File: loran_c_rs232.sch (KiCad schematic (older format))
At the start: 30 parts, among them P301 UART1 3V3, P302 DB9 Ribbon 1, P303 DB9 Ribbon 2, U301 ST3232, U302 ST3232, U303 ST3232

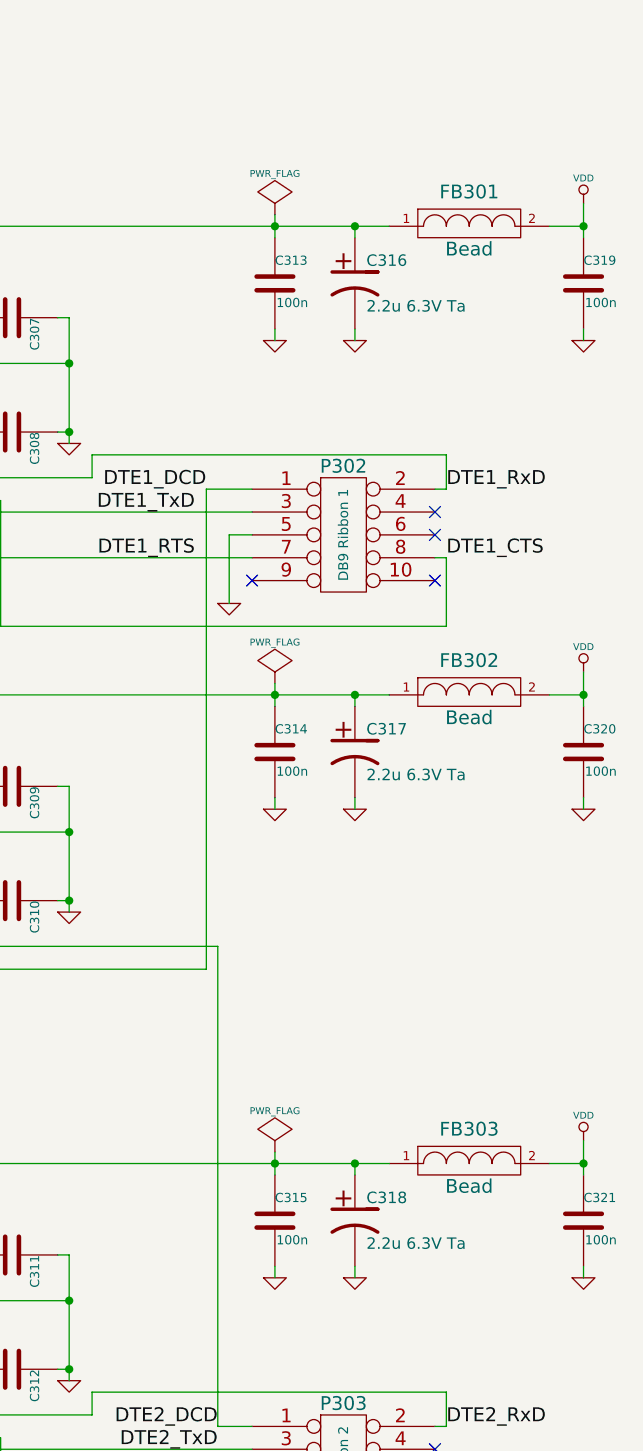
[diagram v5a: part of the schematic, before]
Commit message: Intermediate update: PCB routing/schematic tweaking in process..
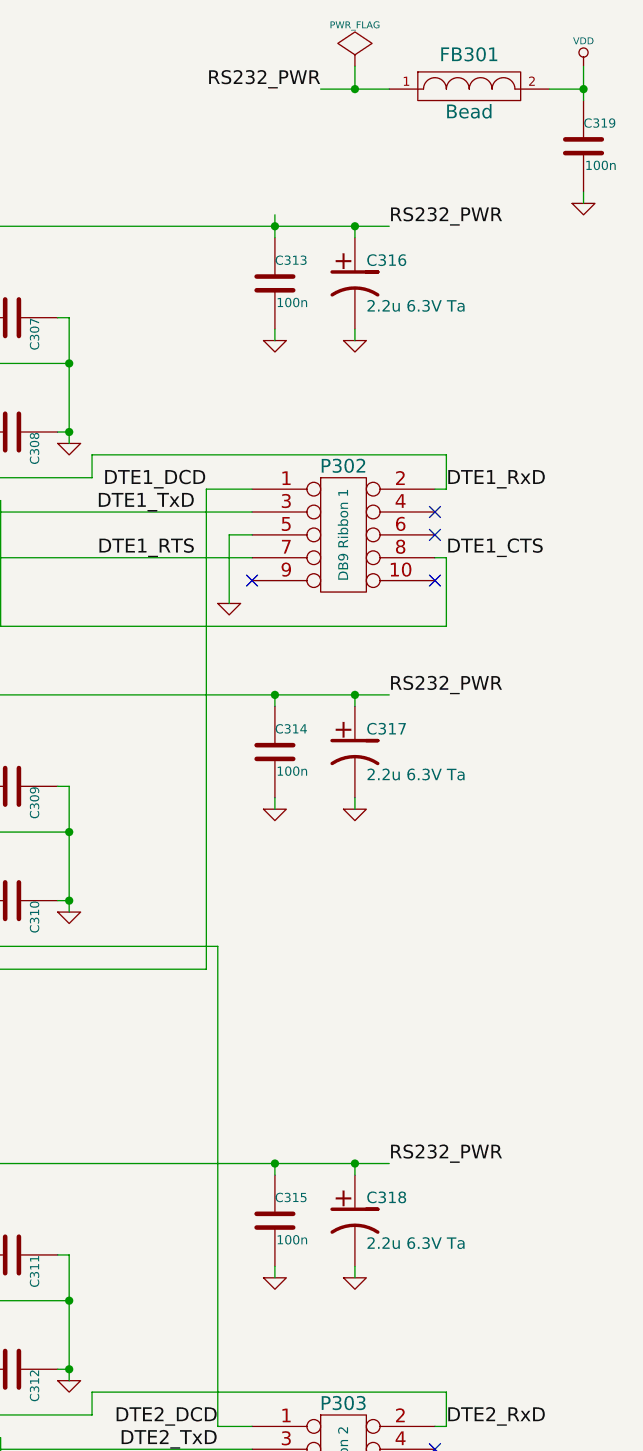
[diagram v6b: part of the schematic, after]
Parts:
- removed C320, C321: 100n, w_smd_capacitors:c_1206, symbol C
- removed FB302, FB303: Bead, w_pth_resistors:RC07, symbol FILTER
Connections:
- net RS232_PWR: now reaches C313.1, C316.1, FB301.1, U301.16 (VCC)
- net RS232_PWR: now also C314.1, C315.1, C317.1, C318.1, U302.16 (VCC), U303.16 (VCC)
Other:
- moved on the sheet: C319, FB301
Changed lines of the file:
@@
 DTE2_CTS
 $Comp
-L GND #PWR057
+L GND #PWR061
 U 1 1 52DBAE37
 P 5600 7750
-F 0 "#PWR057" H 5600 7750 30  0001 C CNN
+F 0 "#PWR061" H 5600 7750 30  0001 C CNN
 F 1 "GND" H 5600 7680 30  0001 C CNN
 F 2 "" H 5600 7750 60  0000 C CNN
@@
 DTE1_CTS
 $Comp
-L GND #PWR058
+L GND #PWR062
 U 1 1 52DBB093
 P 5600 3650
-F 0 "#PWR058" H 5600 3650 30  0001 C CNN
+F 0 "#PWR062" H 5600 3650 30  0001 C CNN
 F 1 "GND" H 5600 3580 30  0001 C CNN
 F 2 "" H 5600 3650 60  0000 C CNN
@@
 $EndComp
 $Comp
-L GND #PWR059
+L GND #PWR063
 U 1 1 52DBC5A6
 P 4900 2950
-F 0 "#PWR059" H 4900 2950 30  0001 C CNN
+F 0 "#PWR063" H 4900 2950 30  0001 C CNN
 F 1 "GND" H 4900 2880 30  0001 C CNN
 F 2 "" H 4900 2950 60  0000 C CNN
@@
 $EndComp
 $Comp
-L GND #PWR060
+L GND #PWR064
 U 1 1 52DBD4A5
 P 4900 7050
-F 0 "#PWR060" H 4900 7050 30  0001 C CNN
+F 0 "#PWR064" H 4900 7050 30  0001 C CNN
 F 1 "GND" H 4900 6980 30  0001 C CNN
 F 2 "" H 4900 7050 60  0000 C CNN
@@
 $EndComp
 $Comp
-L GND #PWR061
+L GND #PWR065
 U 1 1 52DBD9EF
 P 4900 5000
-F 0 "#PWR061" H 4900 5000 30  0001 C CNN
+F 0 "#PWR065" H 4900 5000 30  0001 C CNN
 F 1 "GND" H 4900 4930 30  0001 C CNN
 F 2 "" H 4900 5000 60  0000 C CNN
@@
 $EndComp
 $Comp
-L GND #PWR062
+L GND #PWR066
 U 1 1 52DC08D0
 P 5800 2500
-F 0 "#PWR062" H 5800 2500 30  0001 C CNN
+F 0 "#PWR066" H 5800 2500 30  0001 C CNN
 F 1 "GND" H 5800 2430 30  0001 C CNN
 F 2 "" H 5800 2500 60  0000 C CNN
@@
 $EndComp
 $Comp
-L GND #PWR063
+L GND #PWR067
 U 1 1 52DC08DB
 P 6150 2500
-F 0 "#PWR063" H 6150 2500 30  0001 C CNN
+F 0 "#PWR067" H 6150 2500 30  0001 C CNN
 F 1 "GND" H 6150 2430 30  0001 C CNN
 F 2 "" H 6150 2500 60  0000 C CNN
@@
 L FILTER FB301
 U 1 1 52DC0EC1
-P 6650 2000
-F 0 "FB301" H 6650 2150 60  0000 C CNN
-F 1 "Bead" H 6650 1900 60  0000 C CNN
-F 2 "w_pth_resistors:RC07" H 6650 2000 60  0001 C CNN
-F 3 "" H 6650 2000 60  0000 C CNN
-	1    6650 2000
+P 6650 1400
+F 0 "FB301" H 6650 1550 60  0000 C CNN
+F 1 "Bead" H 6650 1300 60  0000 C CNN
+F 2 "w_pth_resistors:RC07" H 6650 1400 60  0001 C CNN
+F 3 "" H 6650 1400 60  0000 C CNN
+	1    6650 1400
 	1    0    0    -1
 $EndComp
@@
 L C C319
 U 1 1 52DC0F4D
-P 7150 2250
-F 0 "C319" H 7150 2350 40  0000 L CNN
-F 1 "100n" H 7156 2165 40  0000 L CNN
-F 2 "w_smd_capacitors:c_1206" H 7188 2100 30  0001 C CNN
-F 3 "" H 7150 2250 60  0000 C CNN
-	1    7150 2250
-	1    0    0    -1
-$EndComp
-$Comp
-L GND #PWR064
+P 7150 1650
+F 0 "C319" H 7150 1750 40  0000 L CNN
+F 1 "100n" H 7156 1565 40  0000 L CNN
+F 2 "w_smd_capacitors:c_1206" H 7188 1500 30  0001 C CNN
+F 3 "" H 7150 1650 60  0000 C CNN
+	1    7150 1650
+	1    0    0    -1
+$EndComp
+$Comp
+L GND #PWR068
 U 1 1 52DC0F53
-P 7150 2500
-F 0 "#PWR064" H 7150 2500 30  0001 C CNN
-F 1 "GND" H 7150 2430 30  0001 C CNN
-F 2 "" H 7150 2500 60  0000 C CNN
-F 3 "" H 7150 2500 60  0000 C CNN
-	1    7150 2500
-	1    0    0    -1
-$EndComp
-Wire Wire Line
-	7150 2450 7150 2500
-Wire Wire Line
-	7000 2000 7150 2000
-Wire Wire Line
-	7150 1900 7150 2050
-Connection ~ 7150 2000
-$Comp
-L VDD #PWR065
-U 1 1 52DC1066
 P 7150 1900
-F 0 "#PWR065" H 7150 2000 30  0001 C CNN
-F 1 "VDD" H 7150 2010 30  0000 C CNN
+F 0 "#PWR068" H 7150 1900 30  0001 C CNN
+F 1 "GND" H 7150 1830 30  0001 C CNN
 F 2 "" H 7150 1900 60  0000 C CNN
 F 3 "" H 7150 1900 60  0000 C CNN
 	1    7150 1900
+	1    0    0    -1
+$EndComp
+Wire Wire Line
+	7150 1850 7150 1900
+Wire Wire Line
+	7000 1400 7150 1400
+Wire Wire Line
+	7150 1300 7150 1450
+Connection ~ 7150 1400
+$Comp
+L VDD #PWR069
+U 1 1 52DC1066
+P 7150 1300
+F 0 "#PWR069" H 7150 1400 30  0001 C CNN
+F 1 "VDD" H 7150 1410 30  0000 C CNN
+F 2 "" H 7150 1300 60  0000 C CNN
+F 3 "" H 7150 1300 60  0000 C CNN
+	1    7150 1300
 	1    0    0    -1
 $EndComp
@@
 $EndComp
 $Comp
-L GND #PWR066
+L GND #PWR070
 U 1 1 52DC12C1
 P 5800 4550
-F 0 "#PWR066" H 5800 4550 30  0001 C CNN
+F 0 "#PWR070" H 5800 4550 30  0001 C CNN
 F 1 "GND" H 5800 4480 30  0001 C CNN
 F 2 "" H 5800 4550 60  0000 C CNN
@@
 $EndComp
 $Comp
-L GND #PWR067
+L GND #PWR071
 U 1 1 52DC12C7
 P 6150 4550
-F 0 "#PWR067" H 6150 4550 30  0001 C CNN
+F 0 "#PWR071" H 6150 4550 30  0001 C CNN
 F 1 "GND" H 6150 4480 30  0001 C CNN
 F 2 "" H 6150 4550 60  0000 C CNN
@@
 Wire Wire Line
 	6150 4050 6150 4100
-Wire Wire Line
-	5800 4000 5800 4100
 Connection ~ 5800 4050
 Wire Wire Line
@@
 Wire Wire Line
 	6150 4500 6150 4550
-$Comp
-L FILTER FB302
-U 1 1 52DC12D2
-P 6650 4050
-F 0 "FB302" H 6650 4200 60  0000 C CNN
-F 1 "Bead" H 6650 3950 60  0000 C CNN
-F 2 "w_pth_resistors:RC07" H 6650 4050 60  0001 C CNN
-F 3 "" H 6650 4050 60  0000 C CNN
-	1    6650 4050
-	1    0    0    -1
-$EndComp
 Connection ~ 6150 4050
-$Comp
-L C C320
-U 1 1 52DC12D9
-P 7150 4300
-F 0 "C320" H 7150 4400 40  0000 L CNN
-F 1 "100n" H 7156 4215 40  0000 L CNN
-F 2 "w_smd_capacitors:c_1206" H 7188 4150 30  0001 C CNN
-F 3 "" H 7150 4300 60  0000 C CNN
-	1    7150 4300
-	1    0    0    -1
-$EndComp
-$Comp
-L GND #PWR068
-U 1 1 52DC12DF
-P 7150 4550
-F 0 "#PWR068" H 7150 4550 30  0001 C CNN
-F 1 "GND" H 7150 4480 30  0001 C CNN
-F 2 "" H 7150 4550 60  0000 C CNN
-F 3 "" H 7150 4550 60  0000 C CNN
-	1    7150 4550
-	1    0    0    -1
-$EndComp
-Wire Wire Line
-	7150 4500 7150 4550
-Wire Wire Line
-	7000 4050 7150 4050
-Wire Wire Line
-	7150 3950 7150 4100
-Connection ~ 7150 4050
-$Comp
-L VDD #PWR069
-U 1 1 52DC12EA
-P 7150 3950
-F 0 "#PWR069" H 7150 4050 30  0001 C CNN
-F 1 "VDD" H 7150 4060 30  0000 C CNN
-F 2 "" H 7150 3950 60  0000 C CNN
-F 3 "" H 7150 3950 60  0000 C CNN
-	1    7150 3950
-	1    0    0    -1
-$EndComp
 Wire Wire Line
 	4350 6100 6300 6100
@@
 $EndComp
 $Comp
-L GND #PWR070
+L GND #PWR072
 U 1 1 52DC12FF
 P 5800 6600
-F 0 "#PWR070" H 5800 6600 30  0001 C CNN
+F 0 "#PWR072" H 5800 6600 30  0001 C CNN
 F 1 "GND" H 5800 6530 30  0001 C CNN
 F 2 "" H 5800 6600 60  0000 C CNN
@@
 $EndComp
 $Comp
-L GND #PWR071
+L GND #PWR073
 U 1 1 52DC1305
 P 6150 6600
-F 0 "#PWR071" H 6150 6600 30  0001 C CNN
+F 0 "#PWR073" H 6150 6600 30  0001 C CNN
 F 1 "GND" H 6150 6530 30  0001 C CNN
 F 2 "" H 6150 6600 60  0000 C CNN
@@
 Wire Wire Line
 	6150 6100 6150 6150
-Wire Wire Line
-	5800 6050 5800 6150
 Connection ~ 5800 6100
 Wire Wire Line
@@
 Wire Wire Line
 	6150 6550 6150 6600
-$Comp
-L FILTER FB303
-U 1 1 52DC1310
-P 6650 6100
-F 0 "FB303" H 6650 6250 60  0000 C CNN
-F 1 "Bead" H 6650 6000 60  0000 C CNN
-F 2 "w_pth_resistors:RC07" H 6650 6100 60  0001 C CNN
-F 3 "" H 6650 6100 60  0000 C CNN
-	1    6650 6100
-	1    0    0    -1
-$EndComp
 Connection ~ 6150 6100
-$Comp
-L C C321
-U 1 1 52DC1317
-P 7150 6350
-F 0 "C321" H 7150 6450 40  0000 L CNN
-F 1 "100n" H 7156 6265 40  0000 L CNN
-F 2 "w_smd_capacitors:c_1206" H 7188 6200 30  0001 C CNN
-F 3 "" H 7150 6350 60  0000 C CNN
-	1    7150 6350
-	1    0    0    -1
-$EndComp
-$Comp
-L GND #PWR072
-U 1 1 52DC131D
-P 7150 6600
-F 0 "#PWR072" H 7150 6600 30  0001 C CNN
-F 1 "GND" H 7150 6530 30  0001 C CNN
-F 2 "" H 7150 6600 60  0000 C CNN
-F 3 "" H 7150 6600 60  0000 C CNN
-	1    7150 6600
-	1    0    0    -1
-$EndComp
-Wire Wire Line
-	7150 6550 7150 6600
-Wire Wire Line
-	7000 6100 7150 6100
-Wire Wire Line
-	7150 6000 7150 6150
-Connection ~ 7150 6100
-$Comp
-L VDD #PWR073
-U 1 1 52DC1328
-P 7150 6000
-F 0 "#PWR073" H 7150 6100 30  0001 C CNN
-F 1 "VDD" H 7150 6110 30  0000 C CNN
-F 2 "" H 7150 6000 60  0000 C CNN
-F 3 "" H 7150 6000 60  0000 C CNN
-	1    7150 6000
-	1    0    0    -1
-$EndComp
 Wire Wire Line
 	4350 4050 6300 4050
@@
 L PWR_FLAG #FLG075
 U 1 1 52E7FFCD
-P 5800 1950
-F 0 "#FLG075" H 5800 2045 30  0001 C CNN
-F 1 "PWR_FLAG" H 5800 2130 30  0000 C CNN
-F 2 "" H 5800 1950 60  0000 C CNN
-F 3 "" H 5800 1950 60  0000 C CNN
-	1    5800 1950
-	1    0    0    -1
-$EndComp
-$Comp
-L PWR_FLAG #FLG076
-U 1 1 52E80075
-P 5800 4000
-F 0 "#FLG076" H 5800 4095 30  0001 C CNN
-F 1 "PWR_FLAG" H 5800 4180 30  0000 C CNN
-F 2 "" H 5800 4000 60  0000 C CNN
-F 3 "" H 5800 4000 60  0000 C CNN
-	1    5800 4000
-	1    0    0    -1
-$EndComp
-$Comp
-L PWR_FLAG #FLG077
-U 1 1 52E8010C
-P 5800 6050
-F 0 "#FLG077" H 5800 6145 30  0001 C CNN
-F 1 "PWR_FLAG" H 5800 6230 30  0000 C CNN
-F 2 "" H 5800 6050 60  0000 C CNN
-F 3 "" H 5800 6050 60  0000 C CNN
-	1    5800 6050
+P 6150 1300
+F 0 "#FLG075" H 6150 1395 30  0001 C CNN
+F 1 "PWR_FLAG" H 6150 1480 30  0000 C CNN
+F 2 "" H 6150 1300 60  0000 C CNN
+F 3 "" H 6150 1300 60  0000 C CNN
+	1    6150 1300
 	1    0    0    -1
 $EndComp
@@
 Wire Wire Line
 	5550 7250 5700 7250
+Text Label 6000 1400 2    60   ~ 0
+RS232_PWR
+Wire Wire Line
+	6300 1400 6000 1400
+Text Label 6300 2000 0    60   ~ 0
+RS232_PWR
+Text Label 6300 4050 0    60   ~ 0
+RS232_PWR
+Wire Wire Line
+	6150 1300 6150 1400
+Connection ~ 6150 1400
+Text Label 6300 6100 0    60   ~ 0
+RS232_PWR
+Wire Wire Line
+	5800 6150 5800 6100
+Wire Wire Line
+	5800 4100 5800 4050
 $EndSCHEMATC

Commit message: Intermediate update #2: PCB routing/schematic tweaking in process
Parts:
- P302: value DB9 Ribbon 1 -> DB9 Ribbon 2
- P303: value DB9 Ribbon 2 -> DB9 Ribbon 1
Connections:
- net DTE1_CTS: now also P303.8, U303.7 (T2OUT); no longer P302.8, U301.7 (T2OUT)
- net DTE1_DCD: now also P303.1, U302.14 (T1OUT); no longer P302.1, U302.7 (T2OUT)
- net DTE1_RTS: now also P303.7, U303.8 (R2IN); no longer P302.7, U301.8 (R2IN)
- net DTE1_RxD: now also P303.2, U303.14 (T1OUT); no longer P302.2, U301.14 (T1OUT)
- net DTE1_TxD: now also P303.3, U303.13 (R1IN); no longer P302.3, U301.13 (R1IN)
- net DTE2_CTS: now also P302.8, U301.7 (T2OUT); no longer P303.8, U303.7 (T2OUT)
- net DTE2_DCD: now also P302.1, U302.7 (T2OUT); no longer P303.1, U302.14 (T1OUT)
- net DTE2_RTS: now also P302.7, U301.8 (R2IN); no longer P303.7, U303.8 (R2IN)
- net DTE2_RxD: now also P302.2, U301.14 (T1OUT); no longer P303.2, U303.14 (T1OUT)
- net DTE2_TxD: now also P302.3, U301.13 (R1IN); no longer P303.3, U303.13 (R1IN)
- net PPS_UART1: now also U302.11 (T1IN); no longer U302.10 (T2IN)
- net PPS_UART2: now also U302.10 (T2IN); no longer U302.11 (T1IN)
- net UART1_CTS: now also P301.3, U303.9 (R2OUT); no longer P301.4, U301.9 (R2OUT)
- net UART1_RTS: now also P301.4, U303.10 (T2IN); no longer P301.3, U301.10 (T2IN)
- net UART1_RX: now also U303.12 (R1OUT); no longer U301.12 (R1OUT)
- net UART1_TX: now also U303.11 (T1IN); no longer U301.11 (T1IN)
- net UART2_CTS: now also U301.9 (R2OUT); no longer U303.9 (R2OUT)
- net UART2_RTS: now also U301.10 (T2IN); no longer U303.10 (T2IN)
- net UART2_RX: now also U301.12 (R1OUT); no longer U303.12 (R1OUT)
- net UART2_TX: now also U301.11 (T1IN); no longer U303.11 (T1IN)
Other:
- moved on the sheet: P301

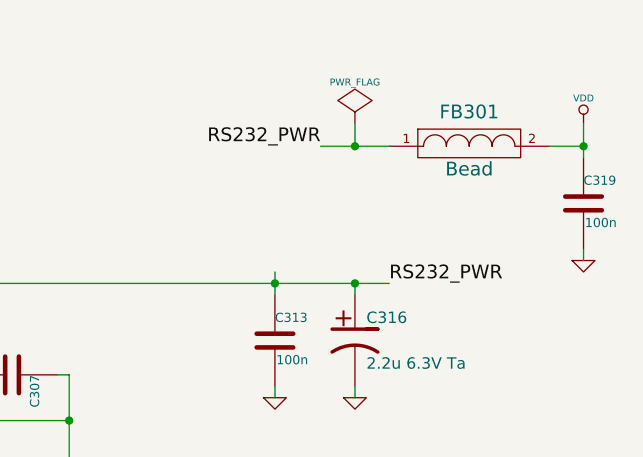
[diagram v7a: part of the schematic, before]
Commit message: Update: lots of refactoring and pin remap ..In chase for easier PCB routing PCB still not completed
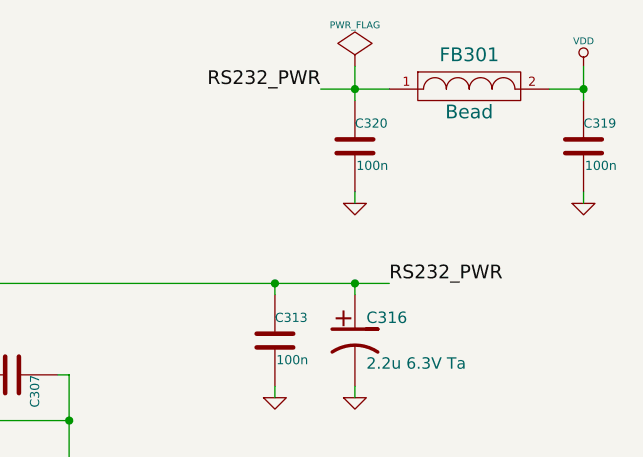
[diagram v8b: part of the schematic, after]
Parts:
- added C320: 100n, w_smd_capacitors:c_1206, symbol C
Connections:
- net GND: now also C320.2
- net RS232_PWR: now also C320.1
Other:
- moved on the sheet: C319, FB301
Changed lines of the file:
@@
 DTE1_CTS
 $Comp
-L GND #PWR064
+L GND #PWR068
 U 1 1 52DBAE37
 P 5600 7750
-F 0 "#PWR064" H 5600 7750 30  0001 C CNN
+F 0 "#PWR068" H 5600 7750 30  0001 C CNN
 F 1 "GND" H 5600 7680 30  0001 C CNN
 F 2 "" H 5600 7750 60  0000 C CNN
@@
 DTE2_CTS
 $Comp
-L GND #PWR065
+L GND #PWR069
 U 1 1 52DBB093
 P 5600 3650
-F 0 "#PWR065" H 5600 3650 30  0001 C CNN
+F 0 "#PWR069" H 5600 3650 30  0001 C CNN
 F 1 "GND" H 5600 3580 30  0001 C CNN
 F 2 "" H 5600 3650 60  0000 C CNN
@@
 $EndComp
 $Comp
-L GND #PWR066
+L GND #PWR070
 U 1 1 52DBC5A6
 P 4900 2950
-F 0 "#PWR066" H 4900 2950 30  0001 C CNN
+F 0 "#PWR070" H 4900 2950 30  0001 C CNN
 F 1 "GND" H 4900 2880 30  0001 C CNN
 F 2 "" H 4900 2950 60  0000 C CNN
@@
 $EndComp
 $Comp
-L GND #PWR067
+L GND #PWR071
 U 1 1 52DBD4A5
 P 4900 7050
-F 0 "#PWR067" H 4900 7050 30  0001 C CNN
+F 0 "#PWR071" H 4900 7050 30  0001 C CNN
 F 1 "GND" H 4900 6980 30  0001 C CNN
 F 2 "" H 4900 7050 60  0000 C CNN
@@
 $EndComp
 $Comp
-L GND #PWR068
+L GND #PWR072
 U 1 1 52DBD9EF
 P 4900 5000
-F 0 "#PWR068" H 4900 5000 30  0001 C CNN
+F 0 "#PWR072" H 4900 5000 30  0001 C CNN
 F 1 "GND" H 4900 4930 30  0001 C CNN
 F 2 "" H 4900 5000 60  0000 C CNN
@@
 $EndComp
 $Comp
-L GND #PWR069
+L GND #PWR073
 U 1 1 52DC08D0
 P 5800 2500
-F 0 "#PWR069" H 5800 2500 30  0001 C CNN
+F 0 "#PWR073" H 5800 2500 30  0001 C CNN
 F 1 "GND" H 5800 2430 30  0001 C CNN
 F 2 "" H 5800 2500 60  0000 C CNN
@@
 $EndComp
 $Comp
-L GND #PWR070
+L GND #PWR074
 U 1 1 52DC08DB
 P 6150 2500
-F 0 "#PWR070" H 6150 2500 30  0001 C CNN
+F 0 "#PWR074" H 6150 2500 30  0001 C CNN
 F 1 "GND" H 6150 2430 30  0001 C CNN
 F 2 "" H 6150 2500 60  0000 C CNN
@@
 L FILTER FB301
 U 1 1 52DC0EC1
-P 6650 1400
-F 0 "FB301" H 6650 1550 60  0000 C CNN
-F 1 "Bead" H 6650 1300 60  0000 C CNN
-F 2 "w_pth_resistors:RC07" H 6650 1400 60  0001 C CNN
-F 3 "" H 6650 1400 60  0000 C CNN
-	1    6650 1400
+P 6650 1150
+F 0 "FB301" H 6650 1300 60  0000 C CNN
+F 1 "Bead" H 6650 1050 60  0000 C CNN
+F 2 "w_pth_resistors:RC07" H 6650 1150 60  0001 C CNN
+F 3 "" H 6650 1150 60  0000 C CNN
+	1    6650 1150
 	1    0    0    -1
 $EndComp
@@
 L C C319
 U 1 1 52DC0F4D
+P 7150 1400
+F 0 "C319" H 7150 1500 40  0000 L CNN
+F 1 "100n" H 7156 1315 40  0000 L CNN
+F 2 "w_smd_capacitors:c_1206" H 7188 1250 30  0001 C CNN
+F 3 "" H 7150 1400 60  0000 C CNN
+	1    7150 1400
+	1    0    0    -1
+$EndComp
+$Comp
+L GND #PWR075
+U 1 1 52DC0F53
 P 7150 1650
-F 0 "C319" H 7150 1750 40  0000 L CNN
-F 1 "100n" H 7156 1565 40  0000 L CNN
-F 2 "w_smd_capacitors:c_1206" H 7188 1500 30  0001 C CNN
+F 0 "#PWR075" H 7150 1650 30  0001 C CNN
+F 1 "GND" H 7150 1580 30  0001 C CNN
+F 2 "" H 7150 1650 60  0000 C CNN
 F 3 "" H 7150 1650 60  0000 C CNN
 	1    7150 1650
@@
 $EndComp
 $Comp
-L GND #PWR071
-U 1 1 52DC0F53
-P 7150 1900
-F 0 "#PWR071" H 7150 1900 30  0001 C CNN
-F 1 "GND" H 7150 1830 30  0001 C CNN
-F 2 "" H 7150 1900 60  0000 C CNN
-F 3 "" H 7150 1900 60  0000 C CNN
-	1    7150 1900
-	1    0    0    -1
-$EndComp
-$Comp
-L VDD #PWR072
+L VDD #PWR076
 U 1 1 52DC1066
-P 7150 1300
-F 0 "#PWR072" H 7150 1400 30  0001 C CNN
-F 1 "VDD" H 7150 1410 30  0000 C CNN
-F 2 "" H 7150 1300 60  0000 C CNN
-F 3 "" H 7150 1300 60  0000 C CNN
-	1    7150 1300
+P 7150 1050
+F 0 "#PWR076" H 7150 1150 30  0001 C CNN
+F 1 "VDD" H 7150 1160 30  0000 C CNN
+F 2 "" H 7150 1050 60  0000 C CNN
+F 3 "" H 7150 1050 60  0000 C CNN
+	1    7150 1050
 	1    0    0    -1
 $EndComp
@@
 $EndComp
 $Comp
-L GND #PWR073
+L GND #PWR077
 U 1 1 52DC12C1
 P 5800 4550
-F 0 "#PWR073" H 5800 4550 30  0001 C CNN
+F 0 "#PWR077" H 5800 4550 30  0001 C CNN
 F 1 "GND" H 5800 4480 30  0001 C CNN
 F 2 "" H 5800 4550 60  0000 C CNN
@@
 $EndComp
 $Comp
-L GND #PWR074
+L GND #PWR078
 U 1 1 52DC12C7
 P 6150 4550
-F 0 "#PWR074" H 6150 4550 30  0001 C CNN
+F 0 "#PWR078" H 6150 4550 30  0001 C CNN
 F 1 "GND" H 6150 4480 30  0001 C CNN
 F 2 "" H 6150 4550 60  0000 C CNN
@@
 $EndComp
 $Comp
-L GND #PWR075
+L GND #PWR079
 U 1 1 52DC12FF
 P 5800 6600
-F 0 "#PWR075" H 5800 6600 30  0001 C CNN
+F 0 "#PWR079" H 5800 6600 30  0001 C CNN
 F 1 "GND" H 5800 6530 30  0001 C CNN
 F 2 "" H 5800 6600 60  0000 C CNN
@@
 $EndComp
 $Comp
-L GND #PWR076
+L GND #PWR080
 U 1 1 52DC1305
 P 6150 6600
-F 0 "#PWR076" H 6150 6600 30  0001 C CNN
+F 0 "#PWR080" H 6150 6600 30  0001 C CNN
 F 1 "GND" H 6150 6530 30  0001 C CNN
 F 2 "" H 6150 6600 60  0000 C CNN
@@
 $EndComp
 $Comp
-L GND #PWR077
+L GND #PWR081
 U 1 1 52DC2978
 P 2150 8650
-F 0 "#PWR077" H 2150 8650 30  0001 C CNN
+F 0 "#PWR081" H 2150 8650 30  0001 C CNN
 F 1 "GND" H 2150 8580 30  0001 C CNN
 F 2 "" H 2150 8650 60  0000 C CNN
@@
 UART1_CTS
 $Comp
-L PWR_FLAG #FLG078
+L PWR_FLAG #FLG082
 U 1 1 52E7FFCD
-P 6150 1300
-F 0 "#FLG078" H 6150 1395 30  0001 C CNN
-F 1 "PWR_FLAG" H 6150 1480 30  0000 C CNN
-F 2 "" H 6150 1300 60  0000 C CNN
-F 3 "" H 6150 1300 60  0000 C CNN
-	1    6150 1300
+P 6150 1050
+F 0 "#FLG082" H 6150 1145 30  0001 C CNN
+F 1 "PWR_FLAG" H 6150 1230 30  0000 C CNN
+F 2 "" H 6150 1050 60  0000 C CNN
+F 3 "" H 6150 1050 60  0000 C CNN
+	1    6150 1050
 	1    0    0    -1
 $EndComp
 NoConn ~ 6500 3550
-Text Label 6000 1400 2    60   ~ 0
+Text Label 6000 1150 2    60   ~ 0
 RS232_PWR
 Text Label 6300 2000 0    60   ~ 0
@@
 Wire Wire Line
 	6150 2000 6150 2050
-Wire Wire Line
-	5800 1950 5800 2050
 Connection ~ 5800 2000
 Wire Wire Line
@@
 Connection ~ 6150 2000
 Wire Wire Line
-	7150 1850 7150 1900
-Wire Wire Line
-	7000 1400 7150 1400
-Wire Wire Line
-	7150 1300 7150 1450
-Connection ~ 7150 1400
+	7150 1600 7150 1650
+Wire Wire Line
+	7000 1150 7150 1150
+Wire Wire Line
+	7150 1050 7150 1200
+Connection ~ 7150 1150
 Wire Wire Line
 	6150 4050 6150 4100
@@
 	5550 7250 5700 7250
 Wire Wire Line
-	6300 1400 6000 1400
-Wire Wire Line
-	6150 1300 6150 1400
-Connection ~ 6150 1400
+	6000 1150 6300 1150
+Wire Wire Line
+	6150 1050 6150 1200
+Connection ~ 6150 1150
 Wire Wire Line
 	5800 6150 5800 6100
@@
 	2250 7100 2250 5150
 Connection ~ 2250 5150
+$Comp
+L C C320
+U 1 1 52F32ACD
+P 6150 1400
+F 0 "C320" H 6150 1500 40  0000 L CNN
+F 1 "100n" H 6156 1315 40  0000 L CNN
+F 2 "w_smd_capacitors:c_1206" H 6188 1250 30  0001 C CNN
+F 3 "" H 6150 1400 60  0000 C CNN
+	1    6150 1400
+	1    0    0    -1
+$EndComp
+$Comp
+L GND #PWR083
+U 1 1 52F32B61
+P 6150 1650
+F 0 "#PWR083" H 6150 1650 30  0001 C CNN
+F 1 "GND" H 6150 1580 30  0001 C CNN
+F 2 "" H 6150 1650 60  0000 C CNN
+F 3 "" H 6150 1650 60  0000 C CNN
+	1    6150 1650
+	1    0    0    -1
+$EndComp
+Wire Wire Line
+	6150 1600 6150 1650
+Wire Wire Line
+	5800 2050 5800 2000
 $EndSCHEMATC
